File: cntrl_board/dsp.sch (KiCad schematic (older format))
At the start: 75 parts, among them J1 PRG, J27 TP, J28 TP, J29 TP, J30 TP, J31 TP, J32 TP, J33 TP, J34 TP, J35 TP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

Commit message: update xformer soft startup
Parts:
- U2: symbol adau:ADAU1467WBCPZ300 -> controller-rescue:ADAU1467WBCPZ300-adau
- gave numbers to parts that had none: 2
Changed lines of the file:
@@
 $EndDescr
 $Comp
-L adau:ADAU1467WBCPZ300 U2
+L controller-rescue:ADAU1467WBCPZ300-adau U2
 U 2 1 60BE69D1
 P 13600 1800
@@
 Connection ~ 4900 5750
 $Comp
-L adau:ADAU1467WBCPZ300 U2
+L controller-rescue:ADAU1467WBCPZ300-adau U2
 U 1 1 60BE58DD
 P 5050 1200
@@
 Connection ~ 6600 8700
 $Comp
-L Device:Net-Tie_2 NT?
+L Device:Net-Tie_2 NT1
 U 1 1 614731D0
 P 12950 2800
-F 0 "NT?" V 12996 2756 50  0000 R CNN
+F 0 "NT1" V 12996 2756 50  0000 R CNN
 F 1 "NT1" V 12905 2756 50  0000 R CNN
 F 2 "" H 12950 2800 50  0001 C CNN
@@
 P 12950 3250
 AR Path="/60CBC38F/61572478" Ref="C?"  Part="1"
-AR Path="/60BF255D/61572478" Ref="C?"  Part="1"
-F 0 "C?" V 12900 3350 50  0000 C CNN
+AR Path="/60BF255D/61572478" Ref="C9"  Part="1"
+F 0 "C9" V 12900 3350 50  0000 C CNN
 F 1 "0.1" V 13000 3400 50  0000 C CNN
 F 2 "Capacitor_SMD:C_0603_1608Metric_Pad1.08x0.95mm_HandSolder" H 12988 3100 50  0001 C CNN

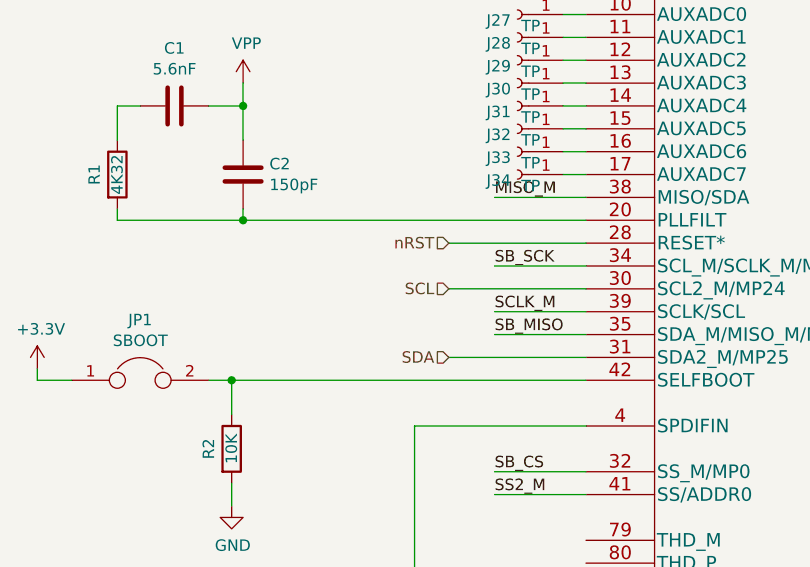
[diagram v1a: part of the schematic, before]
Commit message: fix CPU-DSP channel
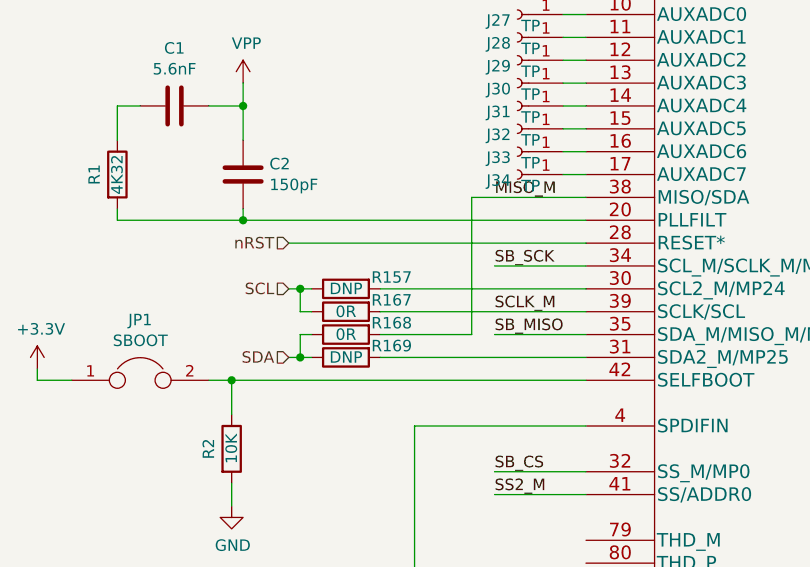
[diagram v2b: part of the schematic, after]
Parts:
- added R157, R169: DNP, Resistor_SMD:R_0603_1608Metric_Pad0.98x0.95mm_HandSolder, symbol Device:R
- added R167, R168: 0R, Resistor_SMD:R_0603_1608Metric_Pad0.98x0.95mm_HandSolder, symbol Device:R
- NT1: footprint (none) -> NetTie:NetTie-2_SMD_Pad0.5mm
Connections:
- net MISO_M: now also R168.2
- net SCL: now also R157.1, R167.1; no longer U2.30 (SCL2_M/MP24)
- net SCLK_M: now also R167.2
- net SDA: now also R168.1, R169.1; no longer U2.31 (SDA2_M/MP25)
- new net: R157.2, U2.30 (SCL2_M/MP24)
- new net: R169.2, U2.31 (SDA2_M/MP25)
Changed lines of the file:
@@
 SB_SCK
-Wire Wire Line
-	5050 3800 4650 3800
 Wire Wire Line
 	8850 3100 8450 3100
@@
 Wire Wire Line
 	13450 2000 13450 2100
-Text HLabel 4450 3900 0    50   Input ~ 0
+Text HLabel 3750 3900 0    50   Input ~ 0
 SDA
-Text HLabel 4450 3600 0    50   Input ~ 0
+Text HLabel 3750 3600 0    50   Input ~ 0
 SCL
-Wire Wire Line
-	5050 3600 4450 3600
-Wire Wire Line
-	5050 3900 4450 3900
-Text HLabel 4450 3400 0    50   Input ~ 0
+Text HLabel 3750 3400 0    50   Input ~ 0
 nRST
-Wire Wire Line
-	4450 3400 5050 3400
 $Comp
 L Device:R R10
@@
 Text Label 14900 9000 2    50   ~ 0
 nRST
-Wire Wire Line
-	5050 3200 4650 3200
 Text Label 4650 3200 0    50   ~ 0
 MISO_M
-Wire Wire Line
-	5050 3700 4650 3700
 Text Label 4650 3700 0    50   ~ 0
 SCLK_M
@@
 F 0 "NT1" V 12996 2756 50  0000 R CNN
 F 1 "NT1" V 12905 2756 50  0000 R CNN
-F 2 "" H 12950 2800 50  0001 C CNN
+F 2 "NetTie:NetTie-2_SMD_Pad0.5mm" H 12950 2800 50  0001 C CNN
 F 3 "~" H 12950 2800 50  0001 C CNN
 	1    12950 2800
@@
 Wire Wire Line
 	12950 3400 12950 3500
+$Comp
+L Device:R R157
+U 1 1 618C71A7
+P 4000 3600
+F 0 "R157" V 3950 3400 50  0000 C CNN
+F 1 "DNP" V 4000 3600 50  0000 C CNN
+F 2 "Resistor_SMD:R_0603_1608Metric_Pad0.98x0.95mm_HandSolder" V 3930 3600 50  0001 C CNN
+F 3 "~" H 4000 3600 50  0001 C CNN
+	1    4000 3600
+	0    -1   1    0
+$EndComp
+$Comp
+L Device:R R167
+U 1 1 618DFC9C
+P 4000 3700
+F 0 "R167" V 3950 3500 50  0000 C CNN
+F 1 "0R" V 4000 3700 50  0000 C CNN
+F 2 "Resistor_SMD:R_0603_1608Metric_Pad0.98x0.95mm_HandSolder" V 3930 3700 50  0001 C CNN
+F 3 "~" H 4000 3700 50  0001 C CNN
+	1    4000 3700
+	0    -1   1    0
+$EndComp
+$Comp
+L Device:R R169
+U 1 1 618F87FD
+P 4000 3900
+F 0 "R169" V 3950 3700 50  0000 C CNN
+F 1 "DNP" V 4000 3900 50  0000 C CNN
+F 2 "Resistor_SMD:R_0603_1608Metric_Pad0.98x0.95mm_HandSolder" V 3930 3900 50  0001 C CNN
+F 3 "~" H 4000 3900 50  0001 C CNN
+	1    4000 3900
+	0    -1   1    0
+$EndComp
+$Comp
+L Device:R R168
+U 1 1 61911366
+P 4000 3800
+F 0 "R168" V 3950 3600 50  0000 C CNN
+F 1 "0R" V 4000 3800 50  0000 C CNN
+F 2 "Resistor_SMD:R_0603_1608Metric_Pad0.98x0.95mm_HandSolder" V 3930 3800 50  0001 C CNN
+F 3 "~" H 4000 3800 50  0001 C CNN
+	1    4000 3800
+	0    -1   1    0
+$EndComp
+Wire Wire Line
+	3850 3600 3800 3600
+Wire Wire Line
+	3850 3700 3800 3700
+Wire Wire Line
+	3800 3700 3800 3600
+Connection ~ 3800 3600
+Wire Wire Line
+	3800 3600 3750 3600
+Wire Wire Line
+	3750 3900 3800 3900
+Wire Wire Line
+	3850 3800 3800 3800
+Wire Wire Line
+	3800 3800 3800 3900
+Connection ~ 3800 3900
+Wire Wire Line
+	3800 3900 3850 3900
+Wire Wire Line
+	5050 3900 4150 3900
+Wire Wire Line
+	5050 3600 4150 3600
+Wire Wire Line
+	4150 3700 5050 3700
+Wire Wire Line
+	5050 3800 4650 3800
+Wire Wire Line
+	4150 3800 4550 3800
+Wire Wire Line
+	4550 3800 4550 3200
+Wire Wire Line
+	4550 3200 5050 3200
+Wire Wire Line
+	3750 3400 5050 3400
 $EndSCHEMATC
